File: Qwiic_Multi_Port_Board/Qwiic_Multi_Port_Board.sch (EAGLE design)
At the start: 4 parts, among them J1 QWIIC_RIGHT_ANGLE, J2 QWIIC_RIGHT_ANGLE, J3 QWIIC_RIGHT_ANGLE, J4 QWIIC_RIGHT_ANGLE

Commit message: Finishing touches
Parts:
- added H1, H2: STAND-OFFTIGHT, SparkFun-Hardware:STAND-OFFTIGHT
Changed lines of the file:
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@@
 <part name="SUPPLY3" library="SparkFun-PowerSymbols" deviceset="3.3V" device=""/>
 <part name="SUPPLY4" library="SparkFun-PowerSymbols" deviceset="3.3V" device=""/>
+<part name="H1" library="SparkFun-Hardware" deviceset="STAND-OFF" device="TIGHT"/>
+<part name="H2" library="SparkFun-Hardware" deviceset="STAND-OFF" device="TIGHT"/>
 </parts>
 <sheets>
@@
 <attribute name="VALUE" x="127" y="104.394" size="1.778" layer="96" align="bottom-center"/>
 </instance>
+<instance part="H1" gate="G$1" x="264.16" y="22.86" smashed="yes"/>
+<instance part="H2" gate="G$1" x="266.7" y="22.86" smashed="yes"/>
 </instances>
 <busses>

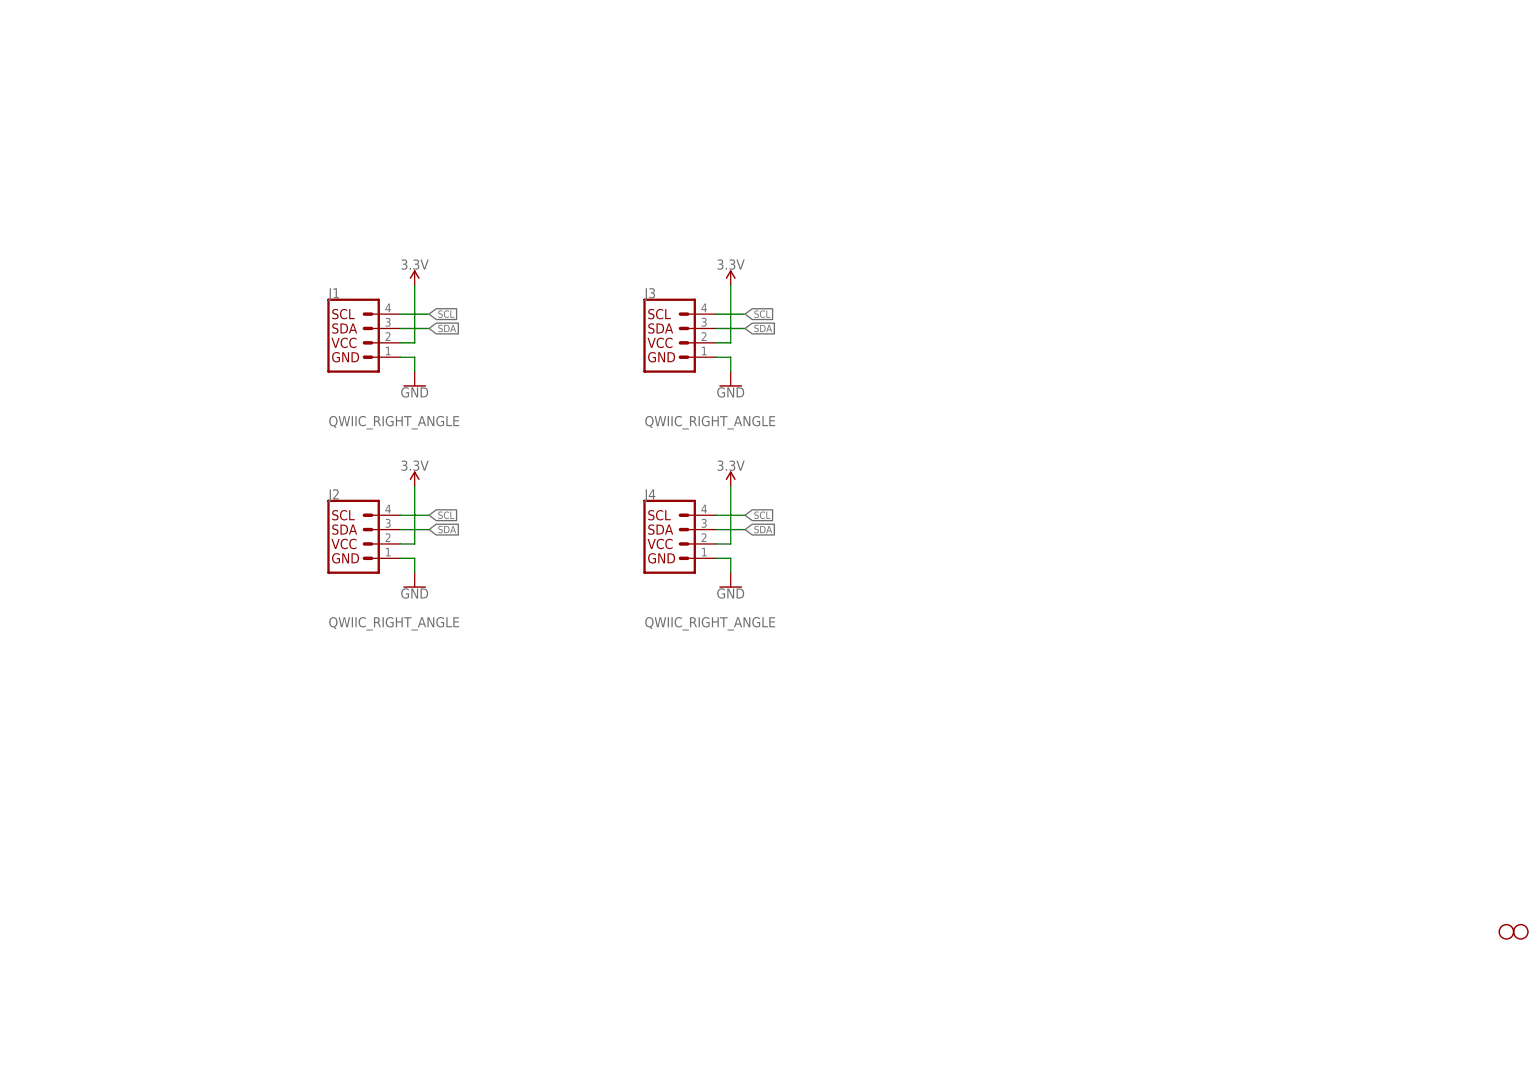
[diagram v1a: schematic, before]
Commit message: Decrease plus width. Move silk. Change to letter frame.
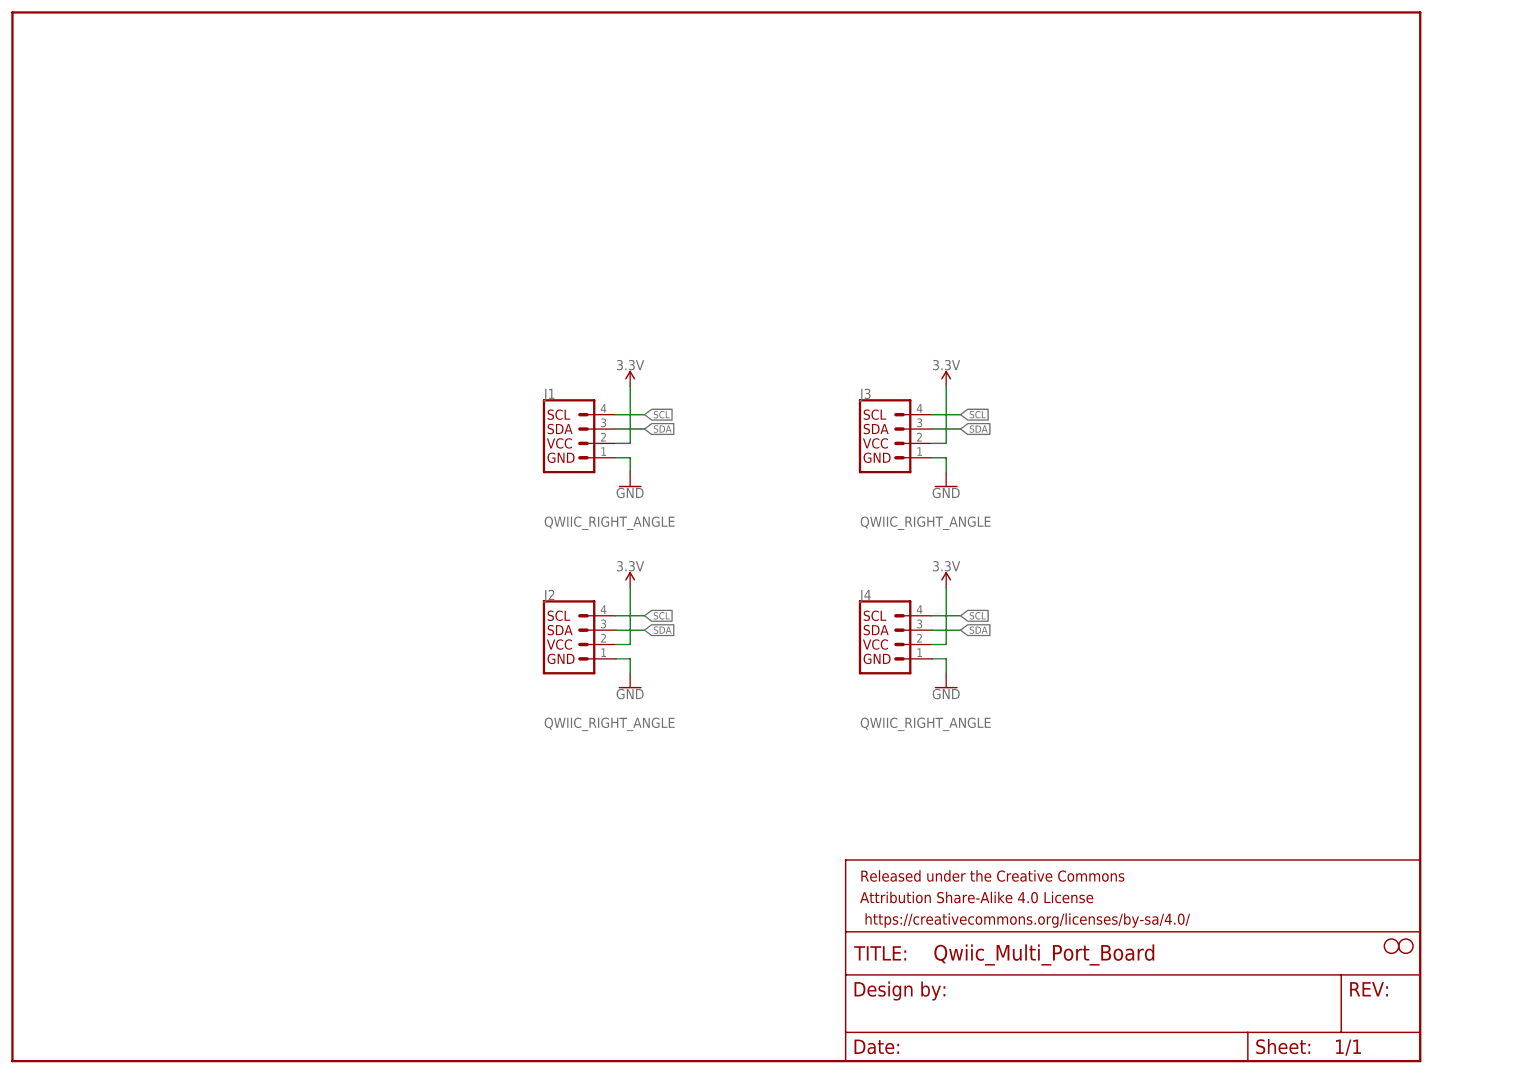
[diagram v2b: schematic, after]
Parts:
- added FRAME1: FRAME-LETTER, SparkFun-Aesthetics:FRAME-LETTER
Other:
- moved on the sheet: J1, J2, J3, J4
